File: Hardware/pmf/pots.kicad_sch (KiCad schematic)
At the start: 40 parts, among them U3 TL074, U4 TL072

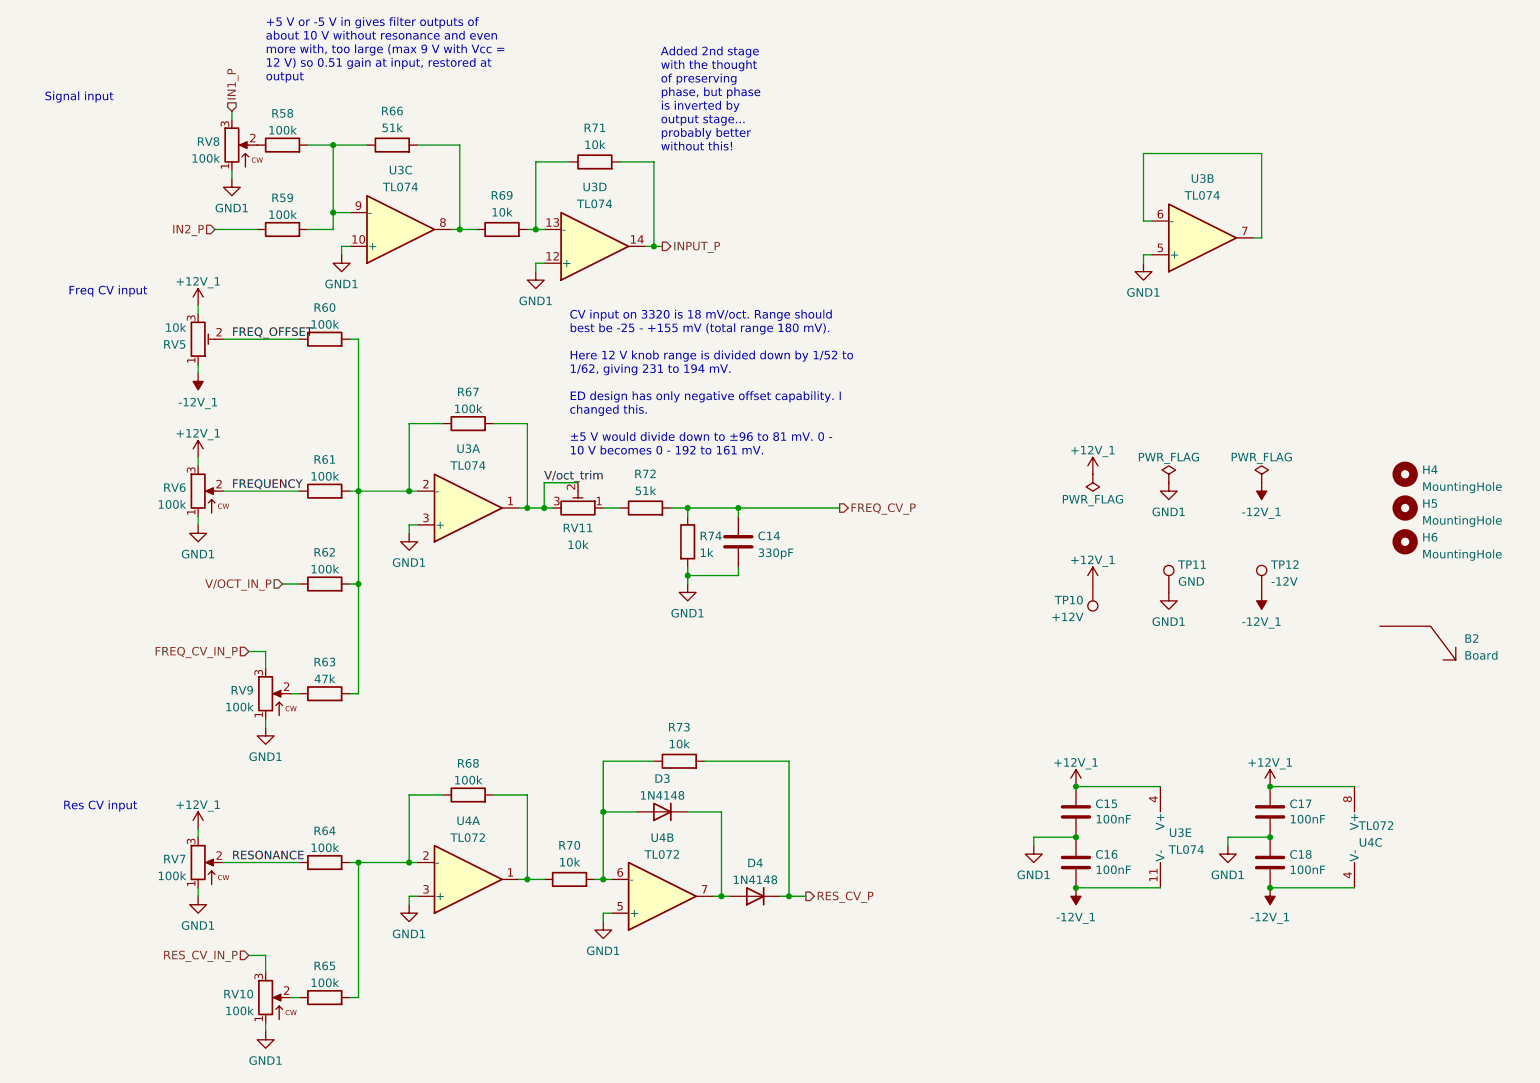
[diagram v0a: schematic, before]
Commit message: Remove second input stage
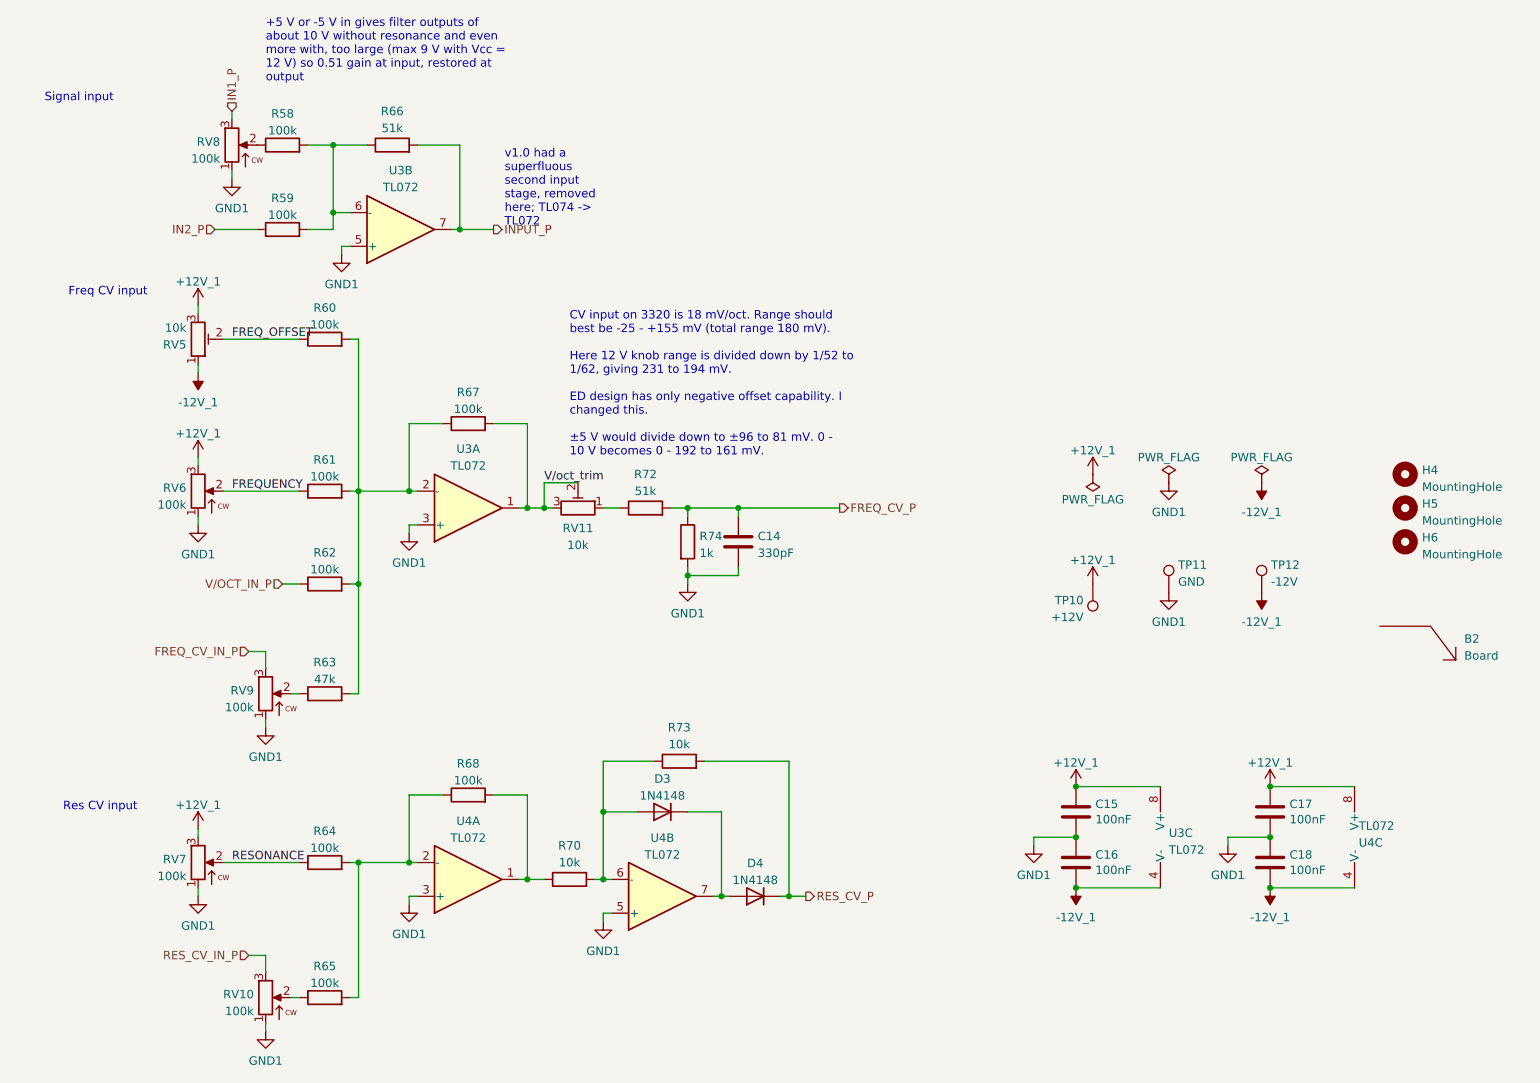
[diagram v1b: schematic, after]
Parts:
- removed R69, R71: 10k, AO_tht:R_Axial_DIN0207_L6.3mm_D2.5mm_P10.16mm_Horizontal, symbol AO_symbols:R
- removed U3: TL074, AO_tht:DIP-14_W7.62mm_Socket_LongPads, symbol AO_symbols:TL074
- added U3: TL072, AO_tht:DIP-8_W7.62mm_Socket_LongPads, symbol AO_symbols:TL072
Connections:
- net +12V_1: now also U3.8 (V+)
- net -12V_1: now also U3.4 (V-)
- net GND1: now also U3.3 (+), U3.5 (+)
- net INPUT_P: now also R66.2, U3.7
- net V/oct_trim: now also U3.1
- net at R60.2, R61.2, R62.2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: now also U3.2 (-)
- net at R58.2, R59.2, R66.1: now also U3.6 (-)
